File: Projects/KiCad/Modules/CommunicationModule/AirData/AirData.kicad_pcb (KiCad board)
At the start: 2 copper layers, 110 x 95 mm, 36 parts, among them J1 Conn_01x08, SW1 SW_DIP_x02, U1 MCP2562-E-P, U2 MCP2515-I/P, U3 NJM7805SDL1, U4 ABX00012, Y1 8MHz

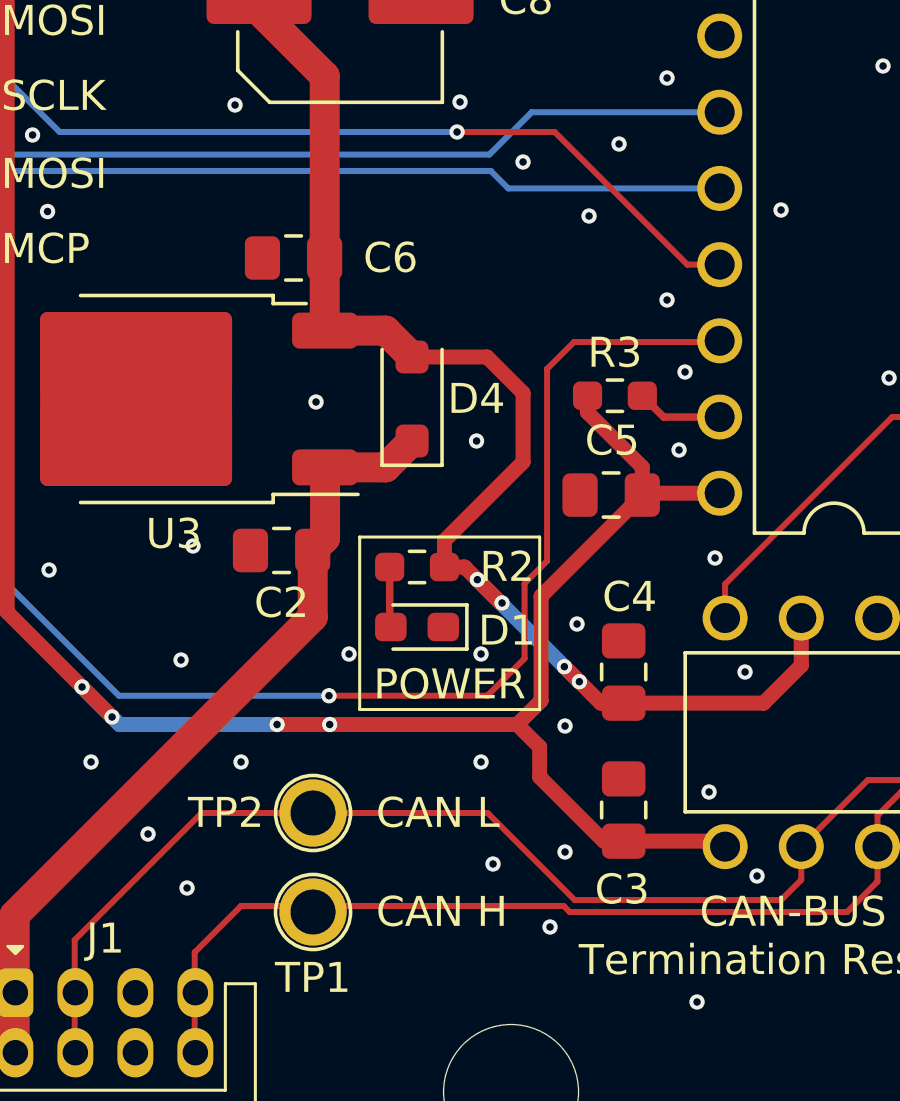
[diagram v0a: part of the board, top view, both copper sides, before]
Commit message: チップ積層セラミックコンデンサをSMD1608に変更
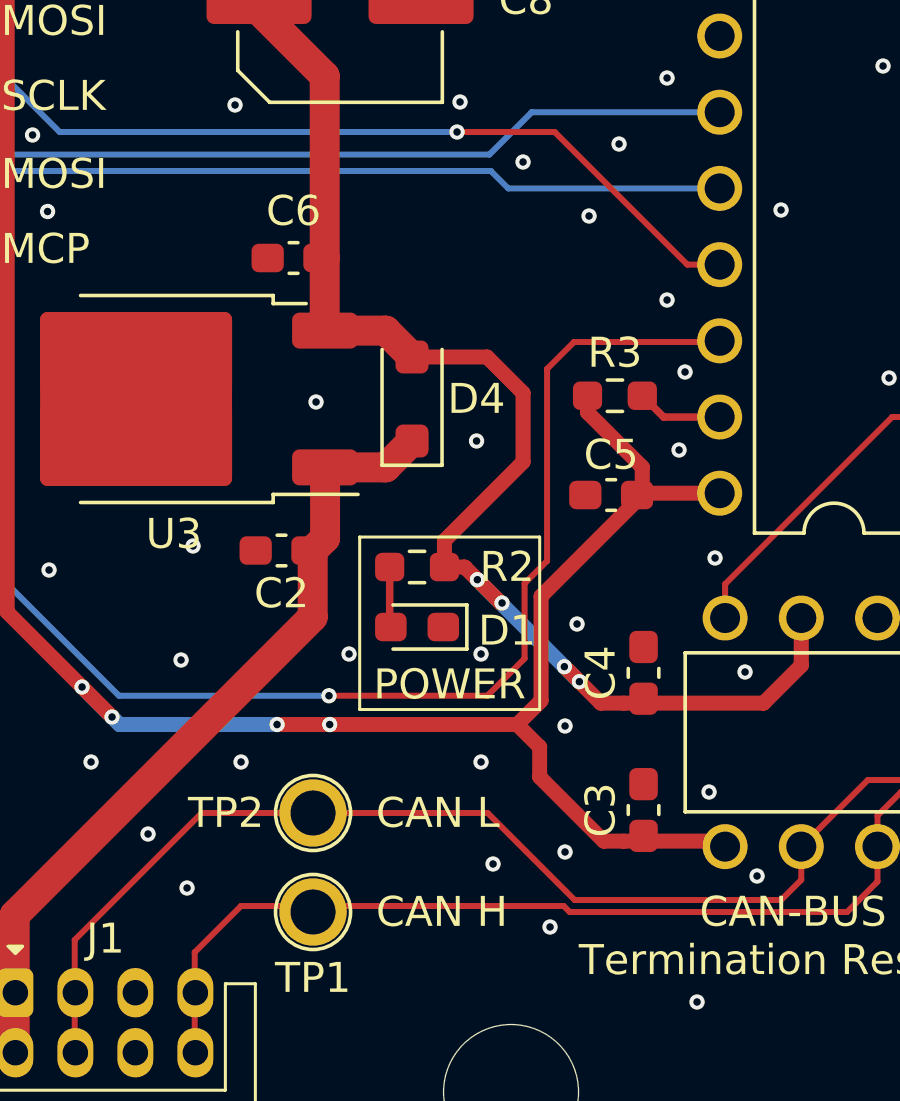
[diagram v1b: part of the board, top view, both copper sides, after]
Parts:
- C2: value 0.33μF -> 10μF; footprint Capacitor_SMD:C_0805_2012Metric_Pad1.18x1.45mm_HandSolder -> Capacitor_SMD:C_0603_1608Metric_Pad1.08x0.95mm_HandSolder
- C3, C4, C5, C6: footprint Capacitor_SMD:C_0805_2012Metric_Pad1.18x1.45mm_HandSolder -> Capacitor_SMD:C_0603_1608Metric_Pad1.08x0.95mm_HandSolder
- moved C4 0.66 mm to (182.9, 121.0)
- moved C3 0.66 mm to (182.9, 125.6)

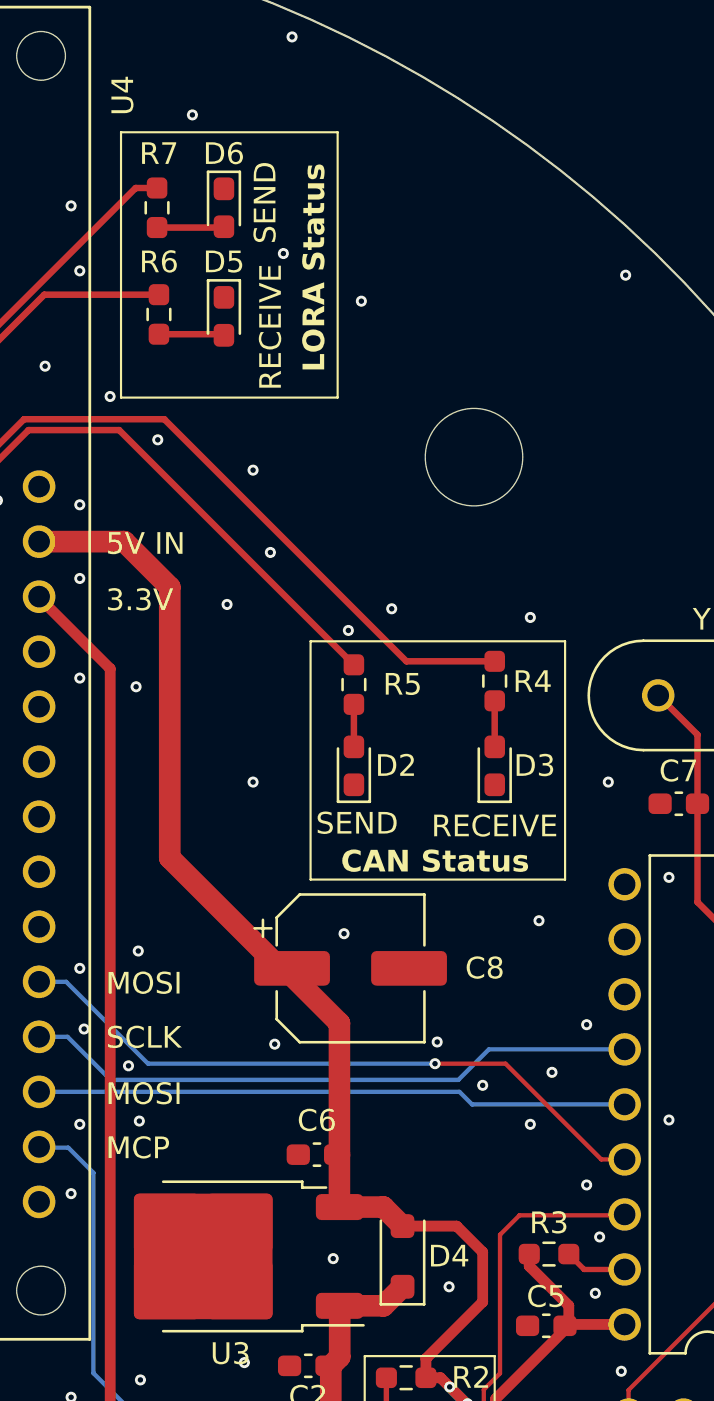
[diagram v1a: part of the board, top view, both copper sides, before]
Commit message: 抵抗の在庫に合わせてサイズを変更
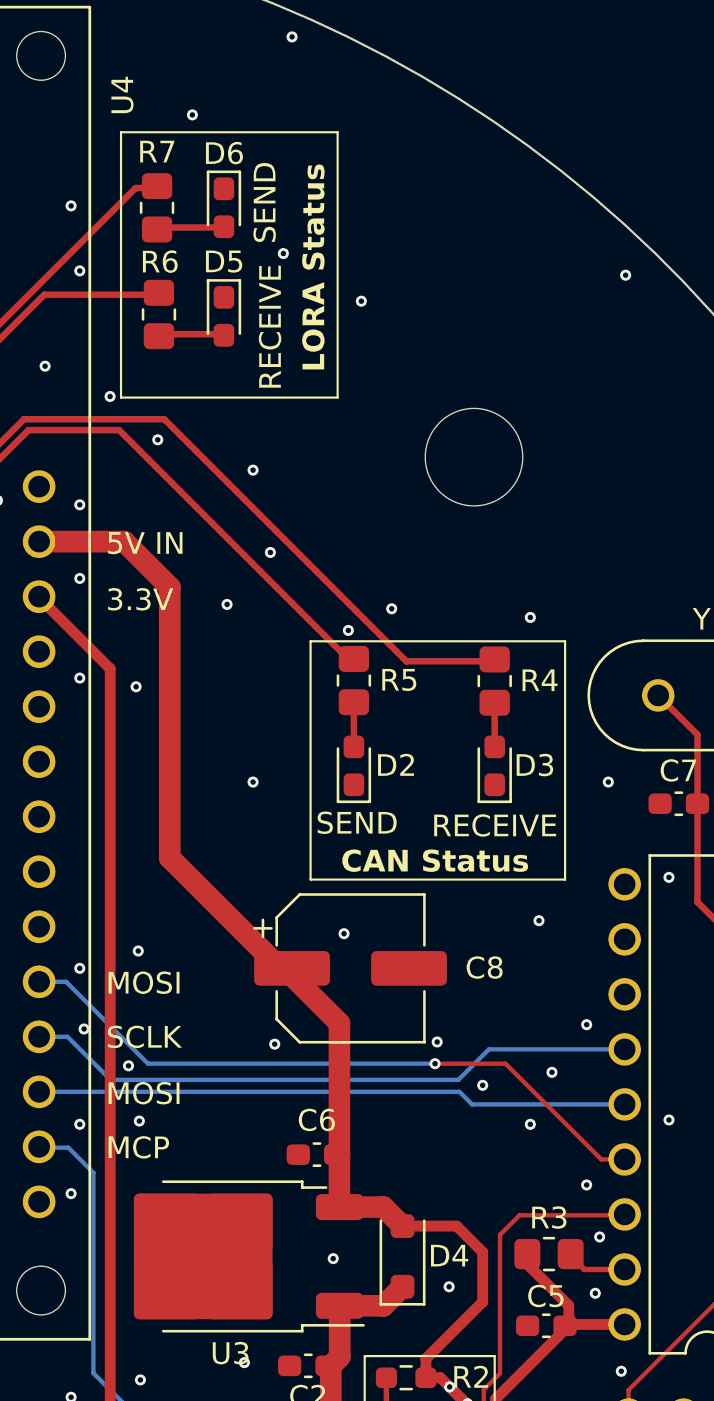
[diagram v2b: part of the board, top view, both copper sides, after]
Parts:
- R3, R4, R5, R6, R7: footprint Resistor_SMD:R_0603_1608Metric_Pad0.98x0.95mm_HandSolder -> Resistor_SMD:R_0805_2012Metric_Pad1.20x1.40mm_HandSolder
- moved R5 0.19 mm to (173.0, 85.3)

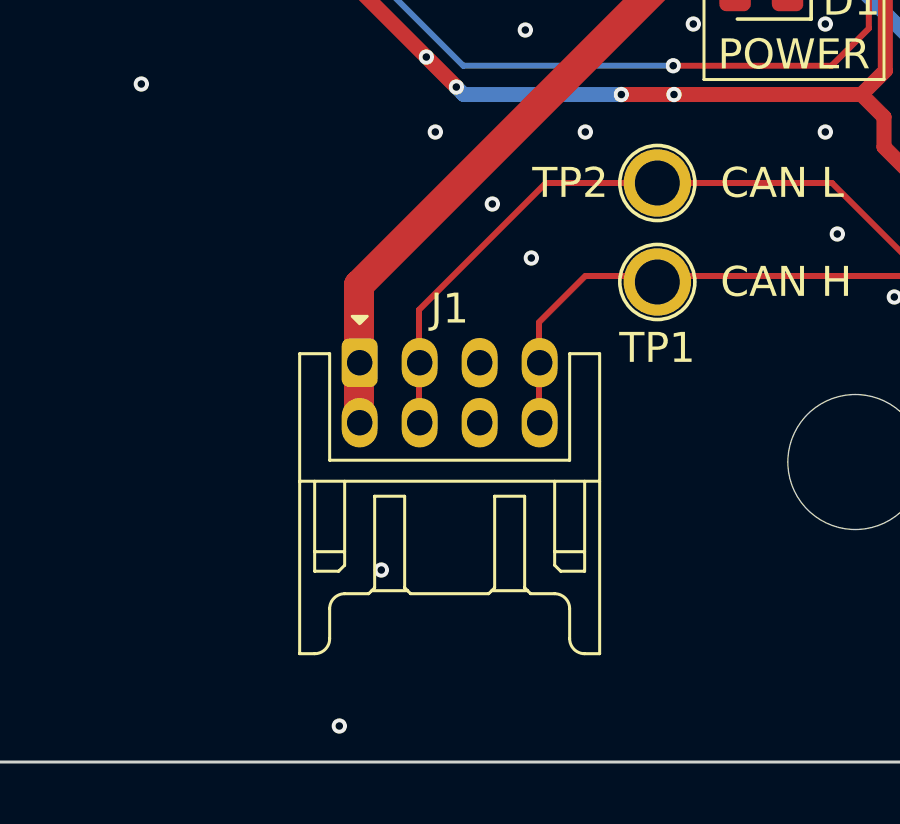
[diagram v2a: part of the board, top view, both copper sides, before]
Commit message: コネクタ位置を揃えた
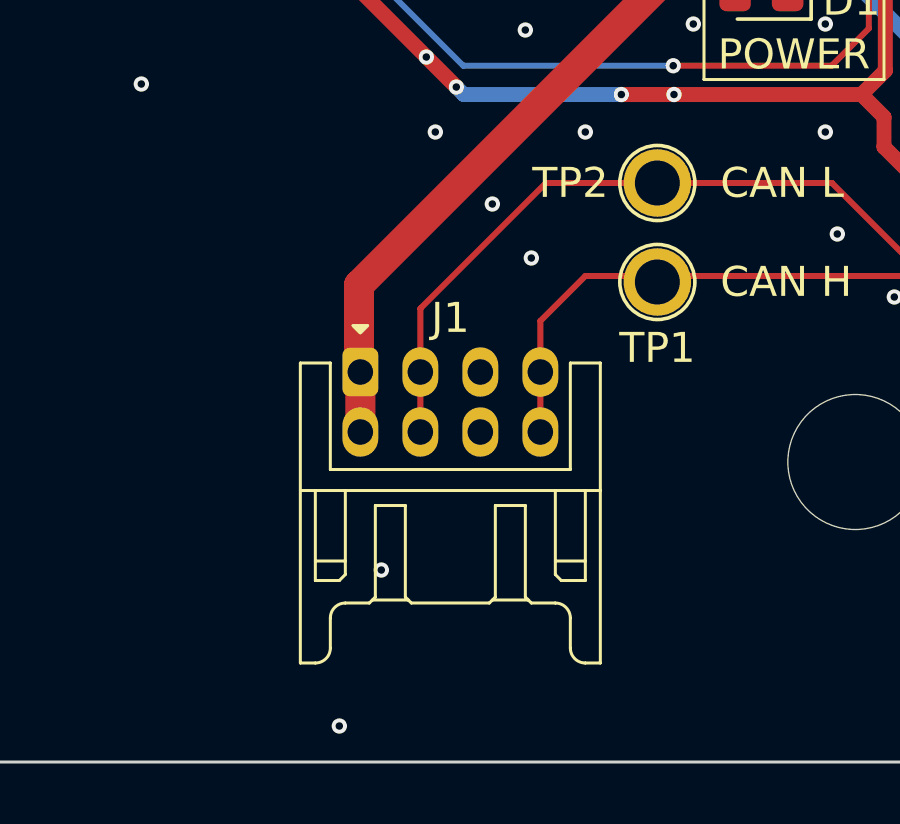
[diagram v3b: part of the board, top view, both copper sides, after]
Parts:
- moved J1 0.31 mm to (162.0, 132.0)

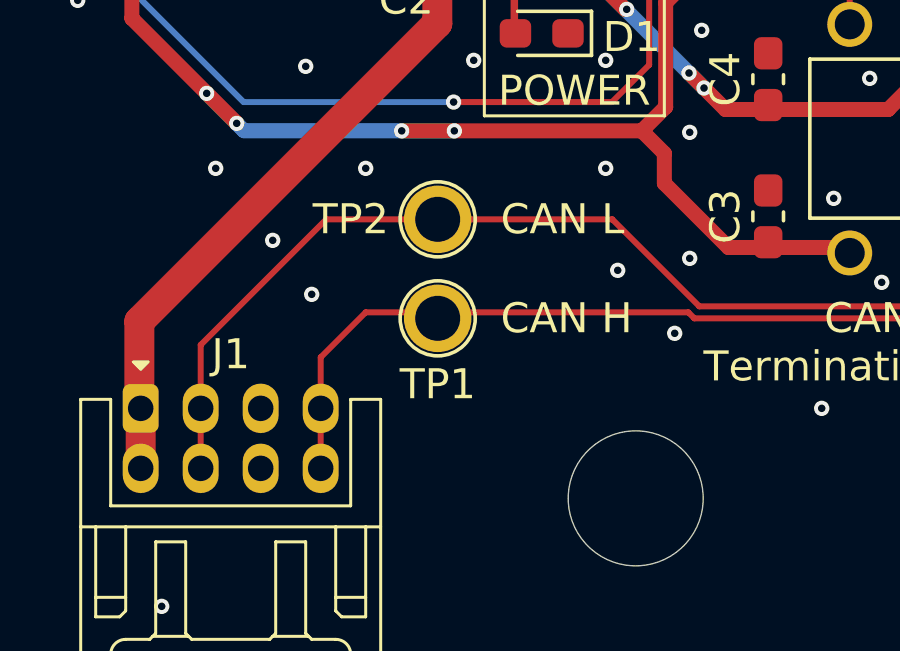
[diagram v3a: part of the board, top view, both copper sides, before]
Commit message: コネクタのピン配置を変更
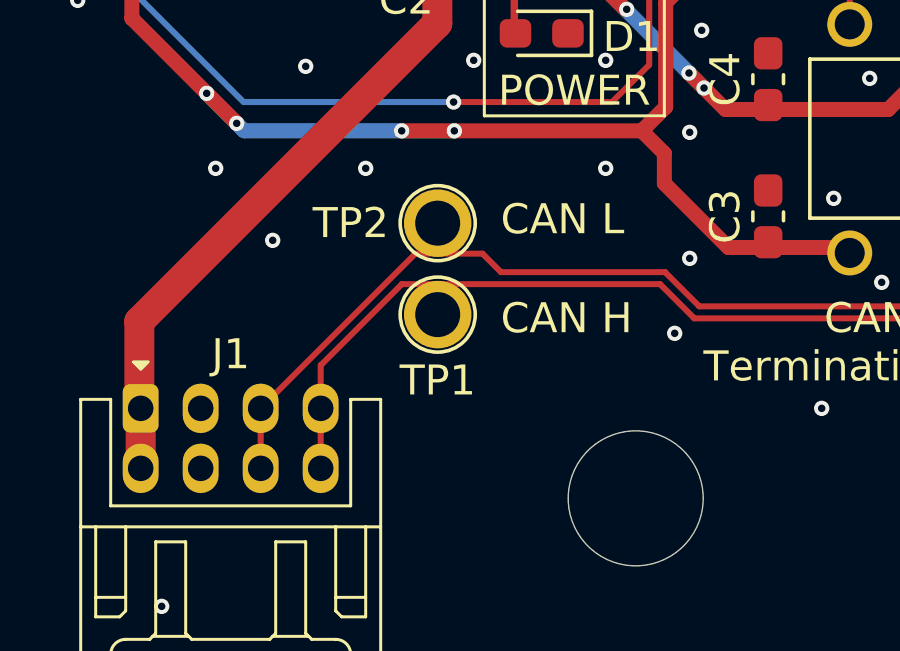
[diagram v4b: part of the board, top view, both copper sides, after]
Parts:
- moved TP2 0.13 mm to (171.9, 125.8)
- moved TP1 0.12 mm to (171.9, 128.9)
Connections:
- J1 pad 3: CAN_L -> GND
- J1 pad 4: CAN_L -> GND
- J1 pad 5: GND -> CAN_L
- J1 pad 6: GND -> CAN_L
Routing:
- net CAN_L: track 45.2 -> 41.0 mm
- net CAN_H: track 39.2 -> 39.8 mm
- net GND: vias 136 -> 134

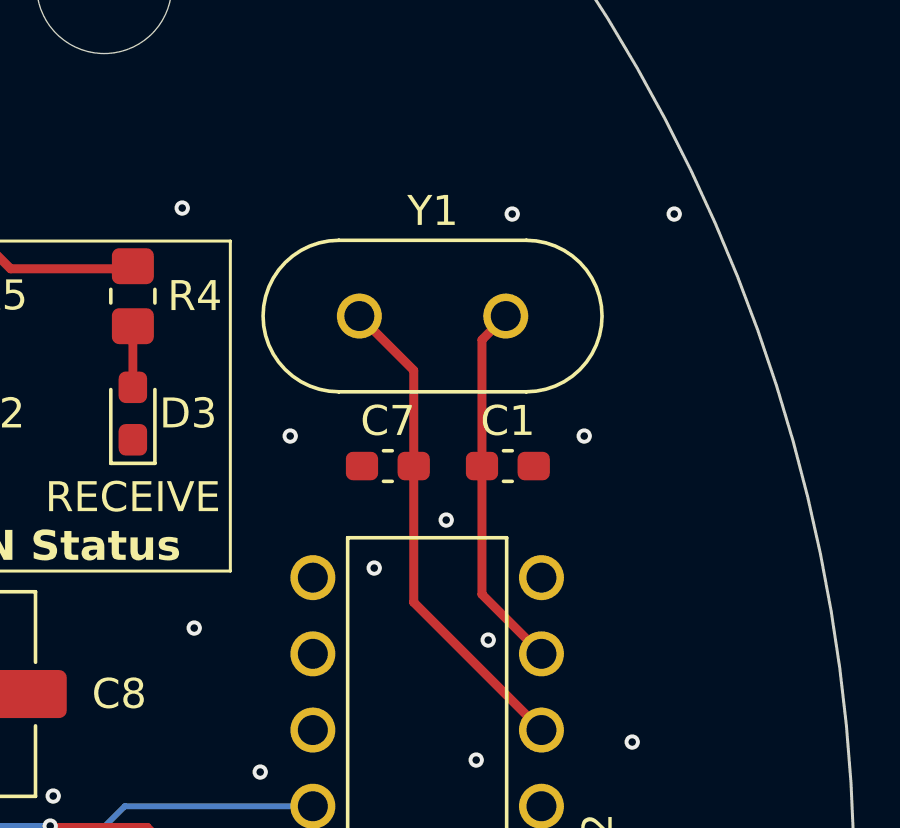
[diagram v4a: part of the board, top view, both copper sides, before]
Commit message: クリスタルをSMDに変更
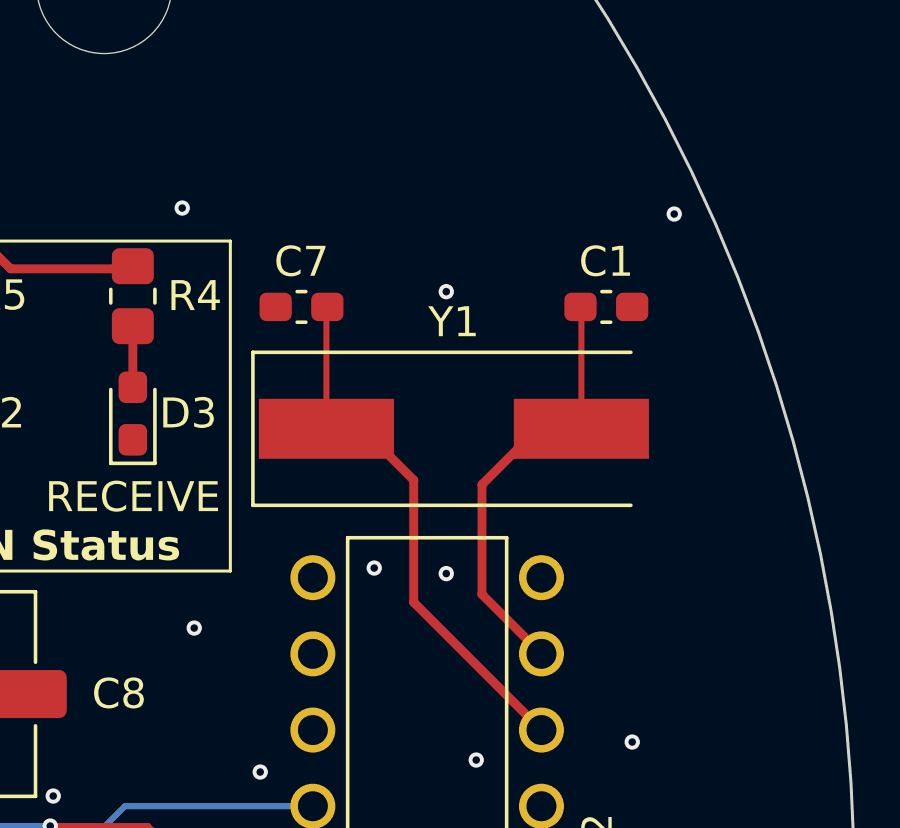
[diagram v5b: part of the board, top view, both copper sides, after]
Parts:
- Y1: footprint Crystal:Crystal_HC49-U_Vertical -> Crystal:Crystal_SMD_HC49-SD
- moved C1 6.24 mm to (195.2, 85.7)
- moved C7 6.04 mm to (185.1, 85.7)
- moved Y1 4.91 mm to (190.2, 89.8)
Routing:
- net OSC1: track 12.4 -> 16.7 mm
- net OSC2: track 16.3 -> 19.2 mm
- net GND: vias 134 -> 131

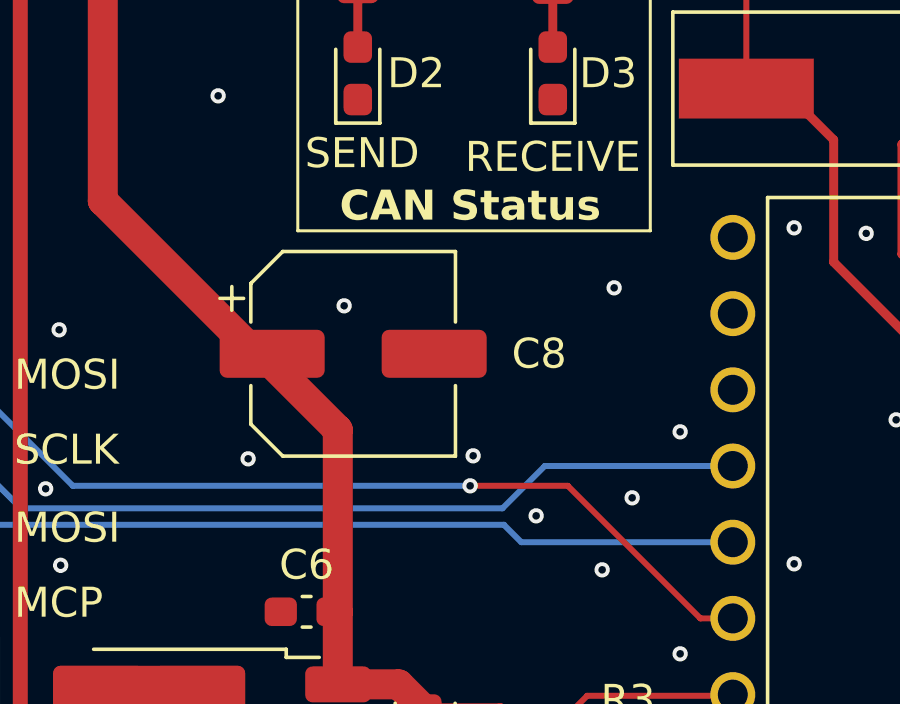
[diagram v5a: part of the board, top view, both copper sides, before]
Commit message: バッファコンデンサを表面実装に変更
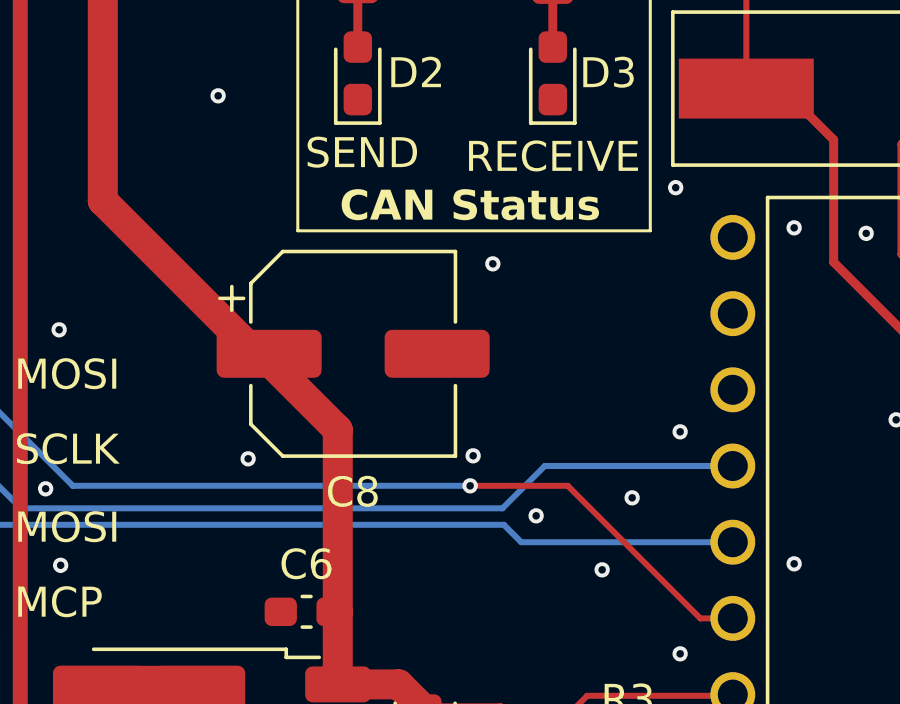
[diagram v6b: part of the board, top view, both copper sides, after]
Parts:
- C8: value 100μF -> 47μF; footprint Capacitor_SMD:CP_Elec_6.3x7.7 -> Capacitor_SMD:CP_Elec_6.3x5.9
